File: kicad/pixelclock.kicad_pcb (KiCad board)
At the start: 2 copper layers, 36.8 x 67.5 mm, 31 parts, among them J1 UART/ISP, J2 LED, J3 USB_B_Micro, J4 5V, J5 LED, Q1 BC848, Q2 BC848, SW1 Reset, U1 ESP32-WROOM-32, U2 SN74LV1T34DBV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

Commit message: Update to KiCad 6
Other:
- net class Default removed
- net class Power removed

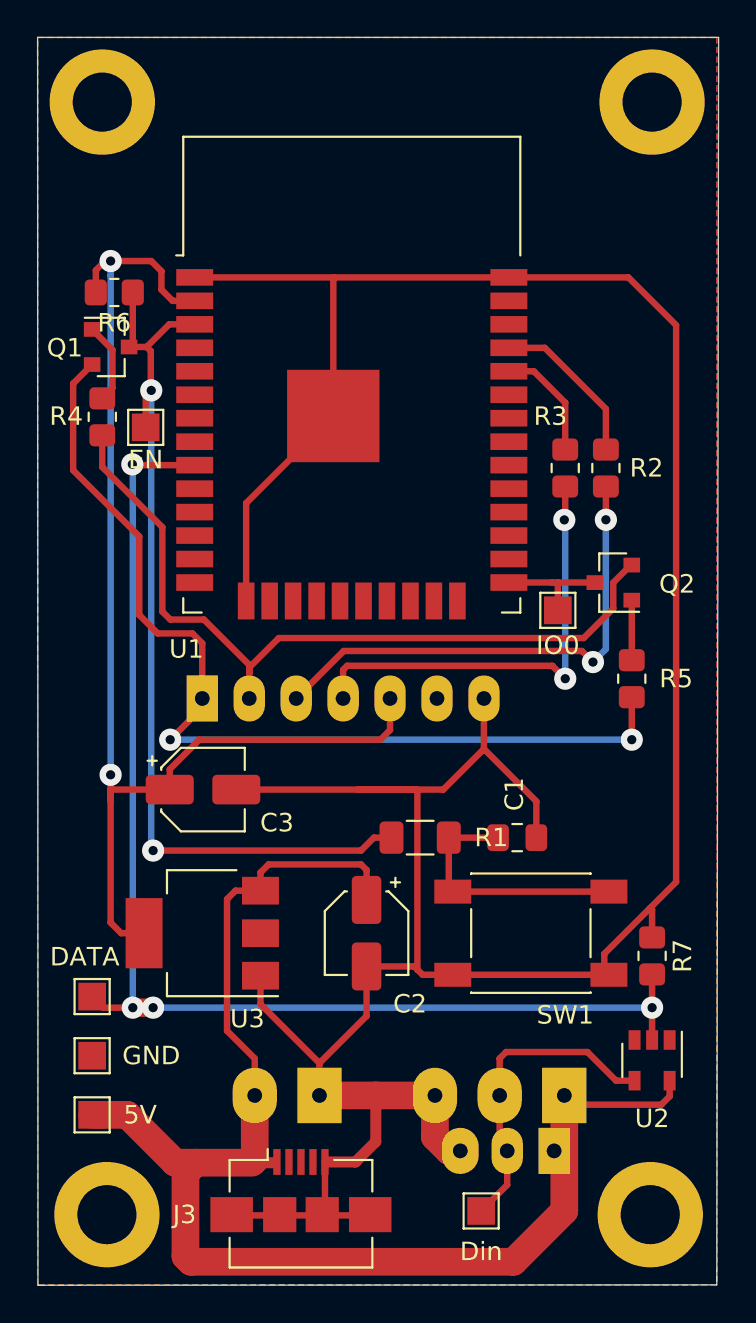
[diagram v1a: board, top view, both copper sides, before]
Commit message: Update pixelclock board to support additional RGBW LED strip (dumb single color LED strip)
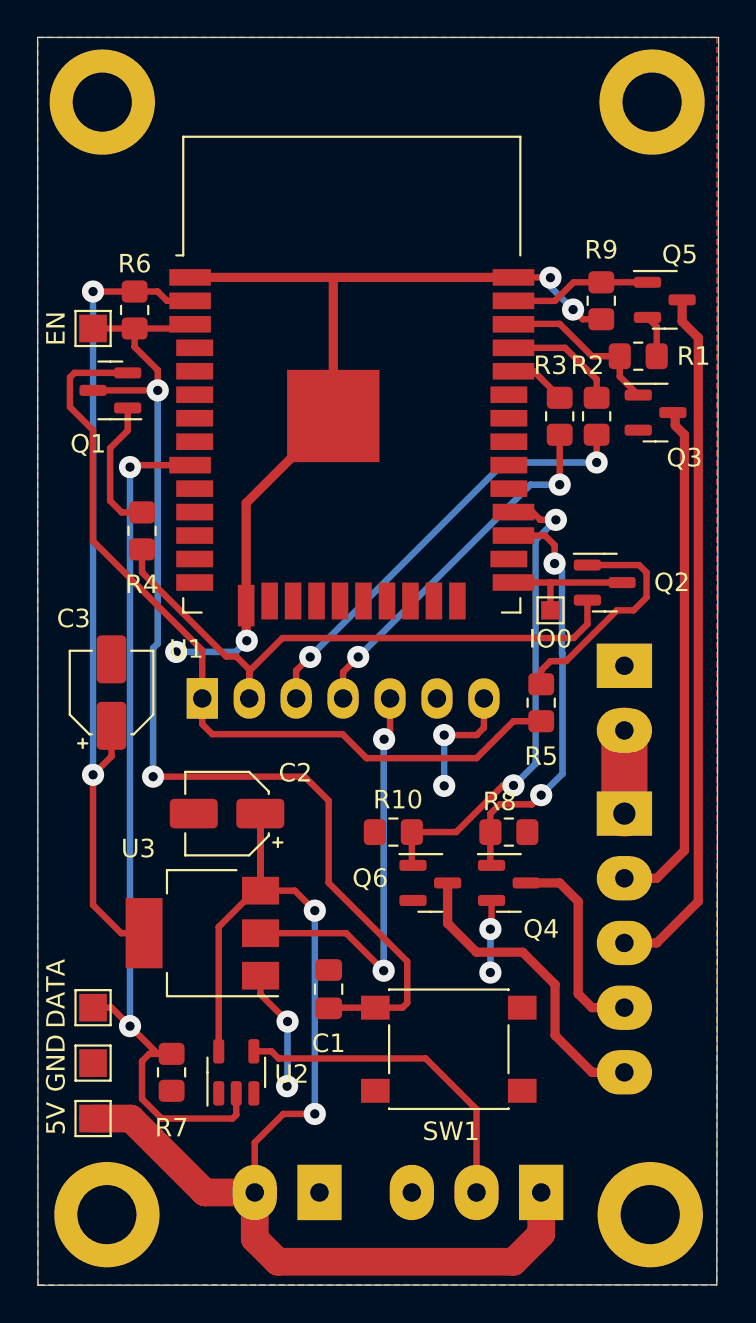
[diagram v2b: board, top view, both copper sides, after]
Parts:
- removed REF**: IO0, TestPoint:TestPoint_Pad_1.5x1.5mm
- removed REF**: Din, TestPoint:TestPoint_Pad_1.5x1.5mm
- removed REF**: EN, TestPoint:TestPoint_Pad_1.5x1.5mm
- removed REF**: DATA, TestPoint:TestPoint_Pad_1.5x1.5mm
- removed REF**: GND, TestPoint:TestPoint_Pad_1.5x1.5mm
- removed REF**: 5V, TestPoint:TestPoint_Pad_1.5x1.5mm
- added Q3: IRLML0030, Package_TO_SOT_SMD:SOT-23, F.Cu at (161.7, 112.8)
- added Q4: IRLML0030, Package_TO_SOT_SMD:SOT-23, F.Cu at (153.8, 138.2)
- added Q5: IRLML0030, Package_TO_SOT_SMD:SOT-23, F.Cu at (162.2, 106.7)
- added Q6: IRLML0030, Package_TO_SOT_SMD:SOT-23, F.Cu at (149.5, 138.2)
- added R10: 1k, Resistor_SMD:R_0805_2012Metric_Pad1.20x1.40mm_HandSolder, F.Cu at (147.5, 135.5)
- added R8: 1k, Resistor_SMD:R_0805_2012Metric_Pad1.20x1.40mm_HandSolder, F.Cu at (153.8, 135.5)
- added R9: 1k, Resistor_SMD:R_0805_2012Metric_Pad1.20x1.40mm_HandSolder, F.Cu at (158.8, 106.8)
- added TP1: 5V, TestPoint:TestPoint_Pad_1.5x1.5mm, F.Cu at (131.2, 151.0)
- added TP2: GND, TestPoint:TestPoint_Pad_1.5x1.5mm, F.Cu at (131.2, 148.0)
- added TP3: DATA, TestPoint:TestPoint_Pad_1.5x1.5mm, F.Cu at (131.2, 145.0)
- added TP4: IO0, TestPoint:TestPoint_Pad_1.0x1.0mm, F.Cu at (156.0, 123.5)
- added TP5: EN, TestPoint:TestPoint_Pad_1.5x1.5mm, F.Cu at (131.2, 108.2)
- J1: footprint Connector_PinSocket_2.54mm:PinSocket_1x07_P2.54mm_Horizontal -> Connector_PinHeader_2.54mm:PinHeader_1x07_P2.54mm_Horizontal
- J2: value LED -> RGBW; footprint Connector_PinSocket_2.54mm:PinSocket_1x03_P2.54mm_Horizontal -> TerminalBlock_Phoenix:TerminalBlock_Phoenix_PT-1,5-5-3.5-H_1x05_P3.50mm_Horizontal
- J3: value USB_B_Micro -> RGBW_Power; footprint Connector_USB:USB_Micro-B_Amphenol_10104110_Horizontal -> TerminalBlock_Phoenix:TerminalBlock_Phoenix_PT-1,5-2-3.5-H_1x02_P3.50mm_Horizontal; moved to B.Cu
- R1: value 0 -> 1k; footprint Resistor_SMD:R_1206_3216Metric_Pad1.30x1.75mm_HandSolder -> Resistor_SMD:R_0805_2012Metric_Pad1.20x1.40mm_HandSolder
- U3: value NCP1117-3.3_SOT223 -> NCP1117-3.3
- moved J3 33.4 mm to (160.0, 126.5), turned to -90 degrees
- moved R1 28.6 mm to (160.8, 109.8)
- moved R7 26.8 mm to (135.5, 148.5), turned to 90 degrees
- moved U2 22.5 mm to (139.0, 148.5), turned to 90 degrees
- moved J2 18.6 mm to (160.0, 134.5), turned to -90 degrees
- moved C1 13.1 mm to (144.0, 144.0), turned to 90 degrees
- moved C2 9.94 mm to (138.5, 134.5), turned to 180 degrees
- moved SW1 7.69 mm to (150.5, 147.2)
- moved C3 7.22 mm to (132.2, 128.0), turned to 90 degrees
- moved R4 6.53 mm to (133.9, 119.2)
- moved J5 5.40 mm to (155.5, 155.0)
- moved J4 5.25 mm to (143.5, 155.0)
- moved R5 5.07 mm to (155.5, 128.5)
- moved R2 2.84 mm to (158.5, 113.0)
- moved R3 2.82 mm to (156.5, 113.0)
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- renumbered REF** to M1, REF** to MH2, REF** to MH3, REF** to MH4
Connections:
- C1 pad 1: Net-(C1-Pad1) -> EN
- J2 pad 1: +5V -> +12V
- J2 pad 2: Din -> POWER_R
- J2 pad 3: GND -> POWER_G
- J3 pad 1: +5V -> GND
- J3 pad 2: D- -> +12V
- R1 pad 1: EN -> RED
- R1 pad 2: Net-(C1-Pad1) -> GND
- SW1 pad 2: Net-(C1-Pad1) -> EN
- U1 pad 10: Net-(U1-Pad10) -> unconnected-(U1-Pad10)
- U1 pad 11: Net-(U1-Pad11) -> unconnected-(U1-Pad11)
- U1 pad 12: Net-(U1-Pad12) -> unconnected-(U1-Pad12)
- U1 pad 13: Net-(U1-Pad13) -> unconnected-(U1-Pad13)
- U1 pad 14: Net-(U1-Pad14) -> unconnected-(U1-Pad14)
- U1 pad 16: Net-(U1-Pad16) -> unconnected-(U1-Pad16)
- U1 pad 17: Net-(U1-Pad17) -> unconnected-(U1-Pad17)
- U1 pad 18: Net-(U1-Pad18) -> unconnected-(U1-Pad18)
- U1 pad 19: Net-(U1-Pad19) -> unconnected-(U1-Pad19)
- U1 pad 20: Net-(U1-Pad20) -> unconnected-(U1-Pad20)
- U1 pad 21: Net-(U1-Pad21) -> unconnected-(U1-Pad21)
- U1 pad 22: Net-(U1-Pad22) -> unconnected-(U1-Pad22)
- U1 pad 23: Net-(U1-Pad23) -> unconnected-(U1-Pad23)
- U1 pad 24: Net-(U1-Pad24) -> unconnected-(U1-Pad24)
- U1 pad 26: Net-(U1-Pad26) -> unconnected-(U1-Pad26)
- U1 pad 27: Net-(U1-Pad27) -> BLUE
- U1 pad 28: Net-(U1-Pad28) -> WHITE
- U1 pad 29: Net-(U1-Pad29) -> unconnected-(U1-Pad29)
- U1 pad 30: Net-(U1-Pad30) -> unconnected-(U1-Pad30)
- U1 pad 31: Net-(U1-Pad31) -> unconnected-(U1-Pad31)
- U1 pad 32: Net-(U1-Pad32) -> unconnected-(U1-Pad32)
- U1 pad 33: Net-(U1-Pad33) -> unconnected-(U1-Pad33)
- U1 pad 36: Net-(U1-Pad36) -> RED
- U1 pad 37: Net-(U1-Pad37) -> GREEN
- U1 pad 4: Net-(U1-Pad4) -> unconnected-(U1-Pad4)
- U1 pad 5: Net-(U1-Pad5) -> unconnected-(U1-Pad5)
- U1 pad 6: Net-(U1-Pad6) -> unconnected-(U1-Pad6)
- U1 pad 7: Net-(U1-Pad7) -> unconnected-(U1-Pad7)
- U1 pad 8: Net-(U1-Pad8) -> unconnected-(U1-Pad8)
- U2 pad 1: Net-(U2-Pad1) -> unconnected-(U2-Pad1)
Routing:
- net GND: track 176.6 -> 68.6 mm, vias 0 -> 10
- net POWER_G: track 0.00 -> 37.8 mm
- net POWER_R: track 0.00 -> 27.8 mm
- net WHITE: track 0.00 -> 26.4 mm, vias 0 -> 2
- net BLUE: track 0.00 -> 22.9 mm, vias 0 -> 2
- net DATA: track 66.9 -> 49.7 mm, vias 4 -> 2
- net POWER_W: track 0.00 -> 16.7 mm
- net Net-(C1-Pad1): track 13.7 -> 0.00 mm
- net EN: track 49.8 -> 61.1 mm
- net POWER_B: track 0.00 -> 11.0 mm
- net DTR: track 42.7 -> 32.9 mm
- net Net-(Q2-Pad1): track 3.25 -> 12.8 mm
- net RED: track 0.00 -> 9.25 mm
- net RTS: track 52.7 -> 44.6 mm, vias 2 -> 0
- net GREEN: track 0.00 -> 7.92 mm
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- added copper zone on B.Cu, net (none)
- removed copper zone on B.Cu, net GND
